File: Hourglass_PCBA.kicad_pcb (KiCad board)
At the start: 2 copper layers, 0.9 x 0.7 mm, 150 parts, among them J1 B2B-PH-SM4-TBLFSN, J2 UJ31-CH-G2-SMT-TR, J3 009159010061911, SW1 KMR221NGLFS, U1 STM32L432KCUx, U2 LP5860, U3 LSM6DSOXTR, U4 MCP1727T-3302E/SN, U5 BQ25185DLHR

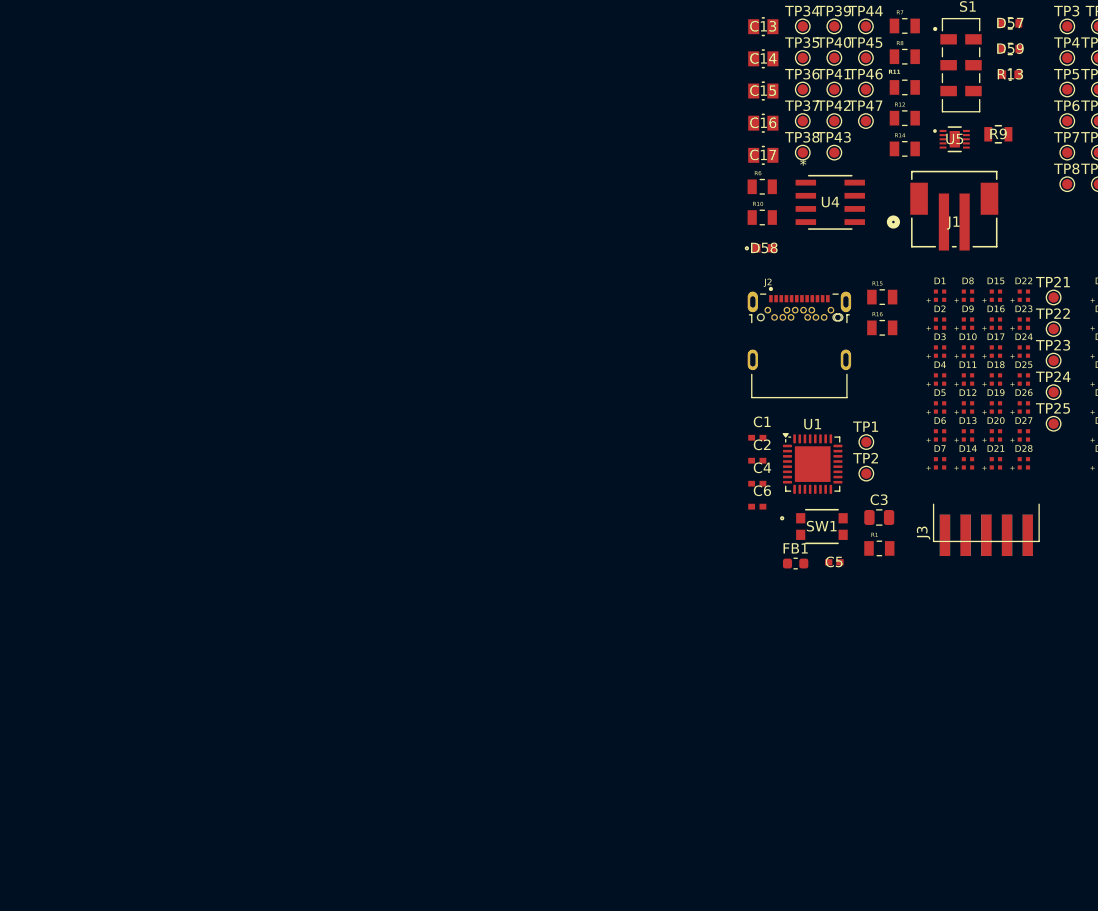
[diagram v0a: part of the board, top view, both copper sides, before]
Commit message: Addressed pull-up on NRST. Added GPIO for  VIO_EN. Added comments on schematic and some TPs
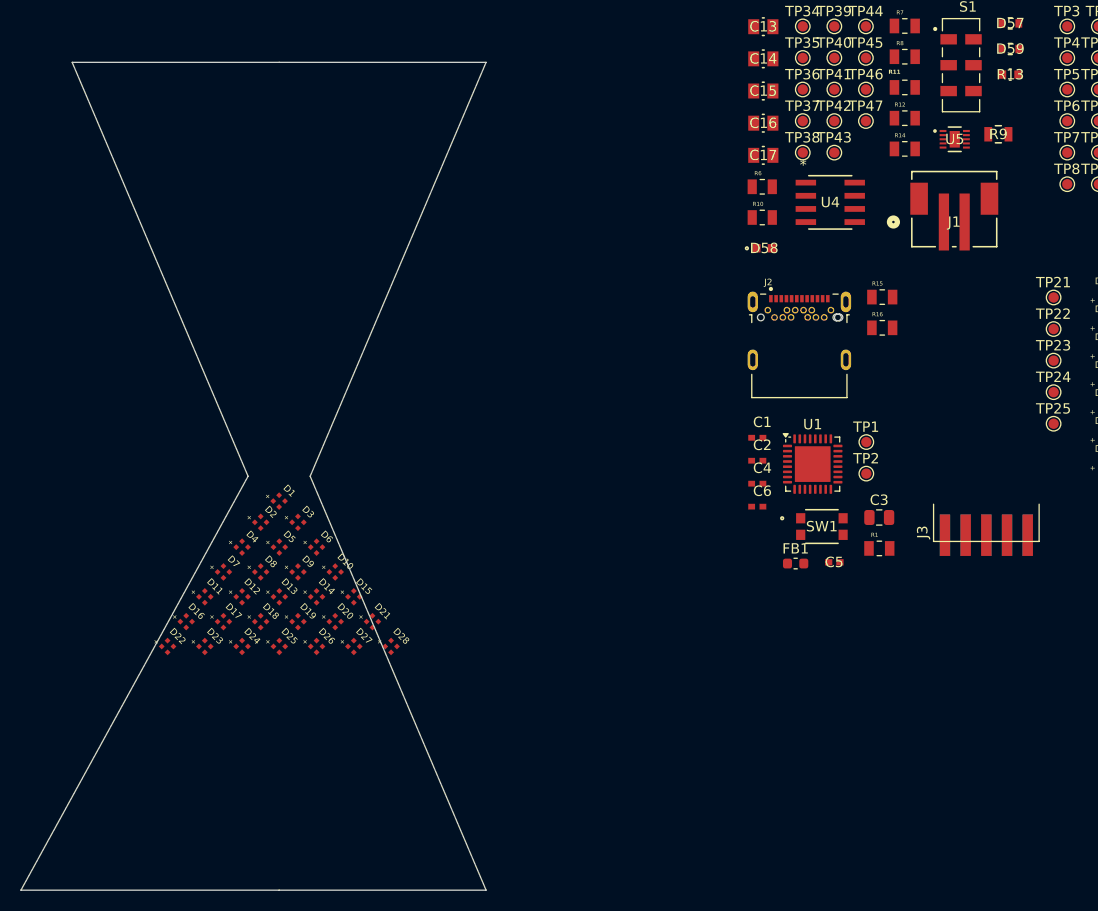
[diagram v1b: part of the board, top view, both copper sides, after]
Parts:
- moved D22 89.4 mm to (189.2, 216.4), turned to -45 degrees
- moved D23 85.1 mm to (192.8, 216.4), turned to -45 degrees
- moved D16 83.4 mm to (191.0, 214.1), turned to -45 degrees
- moved D24 80.7 mm to (196.4, 216.4), turned to -45 degrees
- moved D17 79.1 mm to (194.6, 214.1), turned to -45 degrees
- moved D11 76.7 mm to (192.8, 211.7), turned to -45 degrees
- moved D25 76.4 mm to (200.0, 216.4), turned to -45 degrees
- moved D18 74.8 mm to (198.2, 214.1), turned to -45 degrees
- moved D8 73.4 mm to (198.2, 209.2), turned to -45 degrees
- moved D12 72.5 mm to (196.4, 211.7), turned to -45 degrees
- moved D26 72.1 mm to (203.6, 216.4), turned to -45 degrees
- moved D19 70.6 mm to (201.8, 214.1), turned to -45 degrees
- moved D7 70.0 mm to (194.6, 209.2), turned to -45 degrees
- moved D4 69.4 mm to (196.4, 206.8), turned to -45 degrees
- moved D9 69.1 mm to (201.8, 209.2), turned to -45 degrees
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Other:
- board size 0.9 x 0.7 mm -> 44.9 x 80 mm

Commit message: Re-annotated entire schematic.
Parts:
- added R17: RC0805FR-075K1L, Hourglass_footprint_library:RC0805FR-075K1L, F.Cu at (320.3, 162.8)
- added TP48: TestPoint, TestPoint:TestPoint_Pad_D1.0mm, F.Cu at (316.8, 162.9)
- added TP49: TestPoint, TestPoint:TestPoint_Pad_D1.0mm, F.Cu at (316.8, 165.9)
- added TP50: TestPoint, TestPoint:TestPoint_Pad_D1.0mm, F.Cu at (307.1, 167.1)
- FB1: value FerriteBead_Small -> FCM 1608KF-601T03
- R1: value RMCF0805FT10K0 -> CRCW080518K0FKEAHP; footprint Hourglass_footprint_library:RMCF0805FT10K0 -> Hourglass_footprint_library:CRCW080518K0FKEAHP
- R10: value MCU08050C6000FP500 -> CRCW080518K0FKEAHP; footprint Hourglass_footprint_library:RESC2012X55N -> Hourglass_footprint_library:CRCW080518K0FKEAHP
- R11: value RC0805FR-07442RL -> MCU08050C6000FP500; footprint Hourglass_footprint_library:RC0805FR-07442RL -> Hourglass_footprint_library:RESC2012X55N
- R12: value RMCF0805FT10K0 -> RC0805FR-07442RL; footprint Hourglass_footprint_library:RMCF0805FT10K0 -> Hourglass_footprint_library:RC0805FR-07442RL
- R13: value RC0603JR-07300RL -> RMCF0805FT10K0; footprint Hourglass_footprint_library:RC0603N_YAG -> Hourglass_footprint_library:RMCF0805FT10K0
- R14: value RMCF0805FT10K0 -> RC0603JR-07300RL; footprint Hourglass_footprint_library:RMCF0805FT10K0 -> Hourglass_footprint_library:RC0603N_YAG
- R15: value RC0805FR-075K1L -> RMCF0805FT10K0; footprint Hourglass_footprint_library:RC0805FR-075K1L -> Hourglass_footprint_library:RMCF0805FT10K0
- R2, R3: value RMCF0805FT10K0 -> CRGCQ0805F4K7; footprint Hourglass_footprint_library:RMCF0805FT10K0 -> Hourglass_footprint_library:CRGCQ0805F4K7
- R6: value MCU08050C6000FP500 -> RMCF0805FT10K0; footprint Hourglass_footprint_library:RESC2012X55N -> Hourglass_footprint_library:RMCF0805FT10K0
- R7: value RCS0805300RFKEA -> MCU08050C6000FP500; footprint Hourglass_footprint_library:RCS0805300RFKEA -> Hourglass_footprint_library:RESC2012X55N
- R8: value RCS080513K0FKEA -> RCS0805300RFKEA; footprint Hourglass_footprint_library:RCS080513K0FKEA -> Hourglass_footprint_library:RCS0805300RFKEA
- R9: value CRCW080518K0FKEAHP -> RCS080513K0FKEA; footprint Hourglass_footprint_library:CRCW080518K0FKEAHP -> Hourglass_footprint_library:RCS080513K0FKEA
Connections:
- C9 pad 1: +3V3 -> /LED Driver +  LEDs/VIO_EN
- R1 pad 1: GND -> /MCU/NRST
- R1 pad 2: /MCU/BOOT -> +3V3
- R10 pad 1: Net-(D57-Pad2) -> GND
- R10 pad 2: VCC -> Net-(R10-Pad2)
- R11 pad 1: Net-(D58-Pad2) -> Net-(D57-Pad2)
- R12 pad 1: Net-(U4-PWRGD) -> Net-(D58-Pad2)
- R12 pad 2: +3V3 -> VCC
- R13 pad 1: Net-(D59-Pad1) -> Net-(U4-PWRGD)
- R14 pad 1: GND -> Net-(D59-Pad1)
- R14 pad 2: Net-(U5-TS/MR) -> +3V3
- R15 pad 2: Net-(J2-CC2) -> Net-(U5-TS/MR)
- R16 pad 2: Net-(J2-CC1) -> Net-(J2-CC2)
- R2 pad 1: /LED Driver +  LEDs/I2C.SDA -> /LED Driver +  LEDs/I2C.SCL
- R3 pad 1: /LED Driver +  LEDs/I2C.SCL -> /LED Driver +  LEDs/I2C.SDA
- R4 pad 1: Net-(U3-CS) -> GND
- R4 pad 2: +3V3 -> /MCU/BOOT
- R5 pad 1: GND -> Net-(U3-CS)
- R5 pad 2: Net-(U3-SDO/SA0) -> +3V3
- R6 pad 2: Net-(R6-Pad2) -> Net-(U3-SDO/SA0)
- S1 pad 1: Net-(R6-Pad2) -> Net-(R7-Pad2)
- S1 pad 3: Net-(R7-Pad2) -> Net-(R8-Pad2)
- S1 pad 5: Net-(R9-Pad2) -> Net-(R10-Pad2)
- S1 pad 7: Net-(R8-Pad2) -> Net-(R9-Pad2)
- TP10 pad 1: /LED Driver +  LEDs/CS7 -> /LED Driver +  LEDs/CS13
- TP11 pad 1: /LED Driver +  LEDs/CS8 -> /LED Driver +  LEDs/CS12
- TP12 pad 1: /LED Driver +  LEDs/CS9 -> /LED Driver +  LEDs/CS11
- TP14 pad 1: /LED Driver +  LEDs/CS11 -> /LED Driver +  LEDs/CS9
- TP15 pad 1: /LED Driver +  LEDs/CS12 -> /LED Driver +  LEDs/CS8
- TP16 pad 1: /LED Driver +  LEDs/CS13 -> /LED Driver +  LEDs/CS7
- TP17 pad 1: /LED Driver +  LEDs/CS14 -> /LED Driver +  LEDs/CS6
- TP18 pad 1: /LED Driver +  LEDs/CS15 -> /LED Driver +  LEDs/CS5
- TP19 pad 1: /LED Driver +  LEDs/CS16 -> /LED Driver +  LEDs/CS4
- TP20 pad 1: /LED Driver +  LEDs/CS17 -> /LED Driver +  LEDs/CS3
- TP21 pad 1: /LED Driver +  LEDs/SW0 -> /LED Driver +  LEDs/CS2
- TP22 pad 1: /LED Driver +  LEDs/SW1 -> /LED Driver +  LEDs/CS1
- TP23 pad 1: /LED Driver +  LEDs/SW2 -> /LED Driver +  LEDs/CS0
- TP24 pad 1: /LED Driver +  LEDs/SW3 -> /LED Driver +  LEDs/SW0
- TP25 pad 1: /LED Driver +  LEDs/SW4 -> /LED Driver +  LEDs/SW1
- TP26 pad 1: /LED Driver +  LEDs/SW5 -> /LED Driver +  LEDs/SW2
- TP27 pad 1: /LED Driver +  LEDs/SW6 -> /LED Driver +  LEDs/SW3
- TP28 pad 1: /LED Driver +  LEDs/SW7 -> /LED Driver +  LEDs/SW4
- TP29 pad 1: /LED Driver +  LEDs/SW8 -> /LED Driver +  LEDs/SW5
- TP3 pad 1: /LED Driver +  LEDs/CS0 -> /LED Driver +  LEDs/I2C.SCL
- TP30 pad 1: /LED Driver +  LEDs/SW9 -> /LED Driver +  LEDs/SW6
- TP31 pad 1: /LSM6DSOX 6-Axis IMU/LSM6DSOX_INT2 -> /LED Driver +  LEDs/SW7
- TP32 pad 1: /LSM6DSOX 6-Axis IMU/LSM6DSOX_INT1 -> /LED Driver +  LEDs/SW8
- TP33 pad 1: Net-(U3-CS) -> /LED Driver +  LEDs/SW9
- TP34 pad 1: VCC -> /LSM6DSOX 6-Axis IMU/LSM6DSOX_INT2
- TP35 pad 1: Net-(U5-STAT1) -> /LSM6DSOX 6-Axis IMU/LSM6DSOX_INT1
- TP36 pad 1: GND -> Net-(U3-CS)
- TP37 pad 1: Net-(U5-STAT2) -> VCC
- TP38 pad 1: +3V3 -> Net-(U5-STAT1)
- TP39 pad 1: /Power/ILIM/VSET -> GND
- TP4 pad 1: /LED Driver +  LEDs/CS1 -> /LED Driver +  LEDs/I2C.SDA
- TP40 pad 1: Net-(U4-*SHDN) -> Net-(U5-STAT2)
- TP41 pad 1: /Power/ISET -> +3V3
- TP42 pad 1: Net-(U4-PWRGD) -> /Power/ILIM/VSET
- TP43 pad 1: Net-(U5-BAT) -> Net-(U4-*SHDN)
- TP44 pad 1: GND -> /Power/ISET
- TP45 pad 1: GND -> Net-(U4-PWRGD)
- TP46 pad 1: GND -> Net-(U5-BAT)
- TP5 pad 1: /LED Driver +  LEDs/CS2 -> /LED Driver +  LEDs/VIO_EN
- TP6 pad 1: /LED Driver +  LEDs/CS3 -> /LED Driver +  LEDs/CS17
- TP7 pad 1: /LED Driver +  LEDs/CS4 -> /LED Driver +  LEDs/CS16
- TP8 pad 1: /LED Driver +  LEDs/CS5 -> /LED Driver +  LEDs/CS15
- TP9 pad 1: /LED Driver +  LEDs/CS6 -> /LED Driver +  LEDs/CS14
- U1 pad 28: unconnected-(U1-PB5-Pad28) -> /LED Driver +  LEDs/VIO_EN
- U2 pad 39: +3V3 -> /LED Driver +  LEDs/VIO_EN

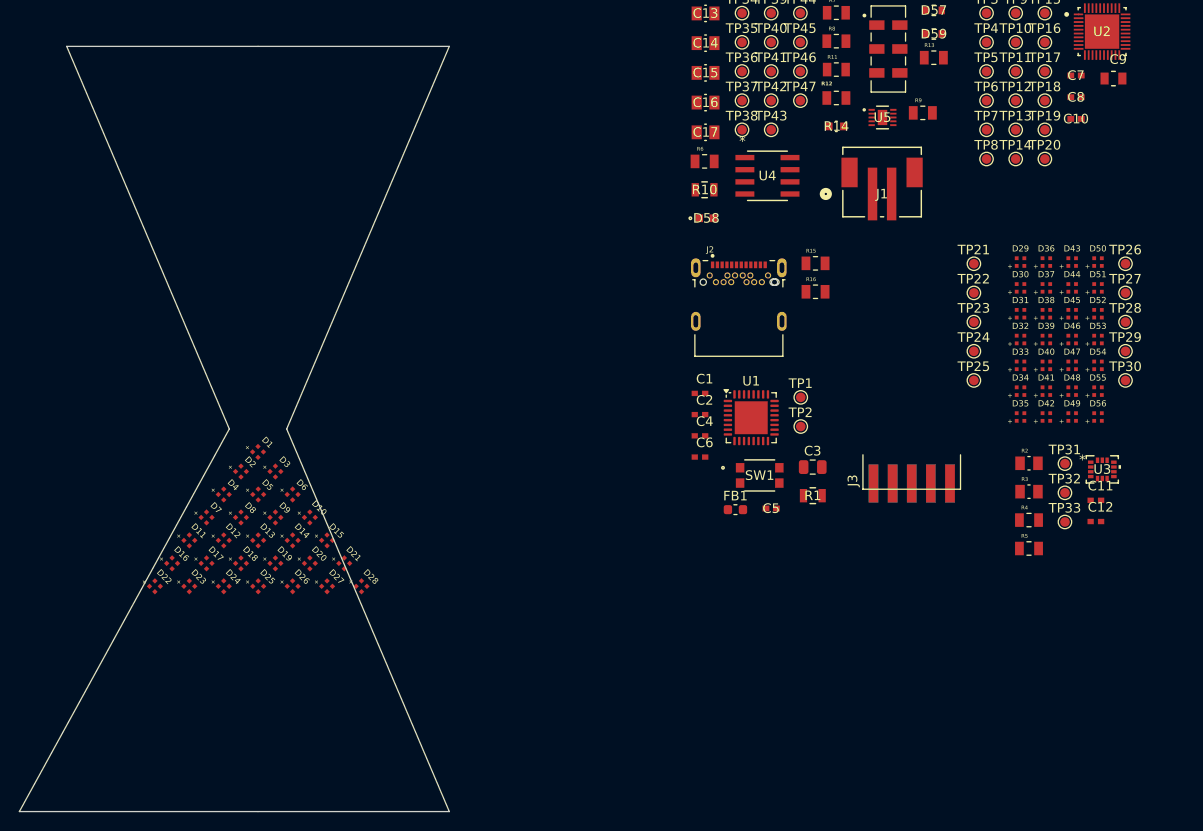
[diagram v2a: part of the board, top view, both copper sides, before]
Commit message: Aligned all LEDs
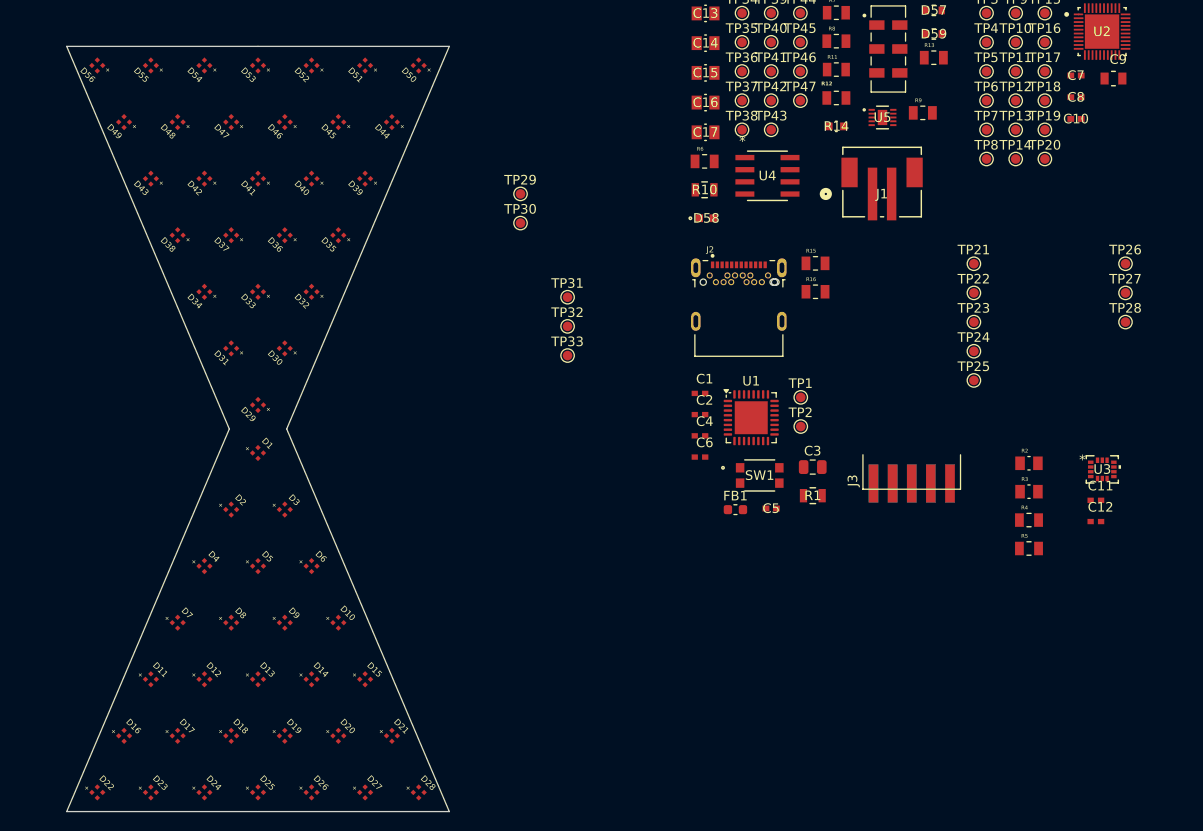
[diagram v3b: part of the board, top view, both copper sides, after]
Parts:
- moved D56 110.9 mm to (183.2, 162.0), turned to 135 degrees
- moved D55 104.7 mm to (188.8, 162.0), turned to 135 degrees
- moved D49 103.8 mm to (186.0, 167.9), turned to 135 degrees
- moved D54 98.5 mm to (194.4, 162.0), turned to 135 degrees
- moved D48 97.7 mm to (191.6, 167.9), turned to 135 degrees
- moved D43 96.7 mm to (188.8, 173.8), turned to 135 degrees
- moved D53 92.4 mm to (200.0, 162.0), turned to 135 degrees
- moved D47 91.5 mm to (197.2, 167.9), turned to 135 degrees
- moved D42 91.5 mm to (194.4, 173.8), turned to 135 degrees
- moved D38 91.2 mm to (191.6, 179.7), turned to 135 degrees
- moved D52 86.2 mm to (205.6, 162.0), turned to 135 degrees
- moved D34 86.0 mm to (194.4, 185.7), turned to 135 degrees
- moved D46 85.4 mm to (202.8, 167.9), turned to 135 degrees
- moved D37 85.4 mm to (197.2, 179.7), turned to 135 degrees
- moved D41 85.4 mm to (200.0, 173.8), turned to 135 degrees
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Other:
- board size 44.9 x 80 mm -> 40 x 80 mm

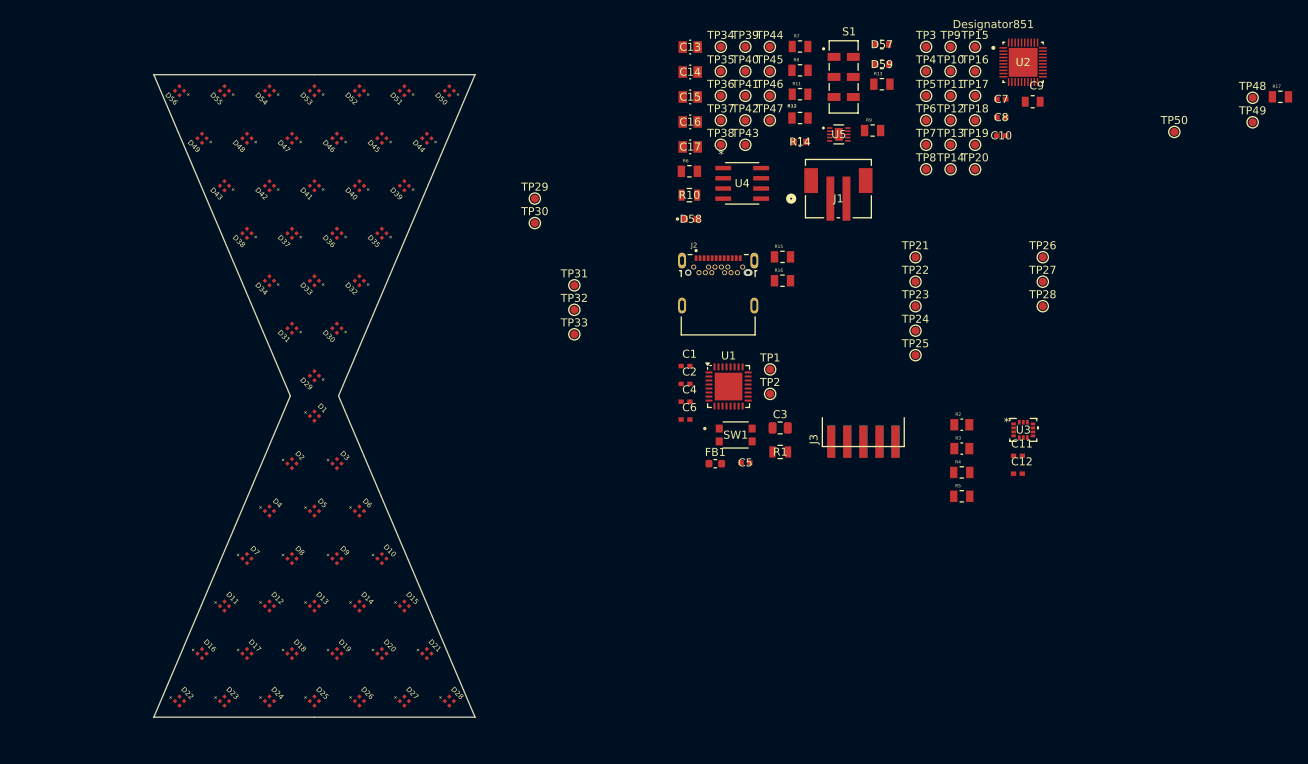
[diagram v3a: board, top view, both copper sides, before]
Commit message: Arranged parts for power- not complete at this commit.
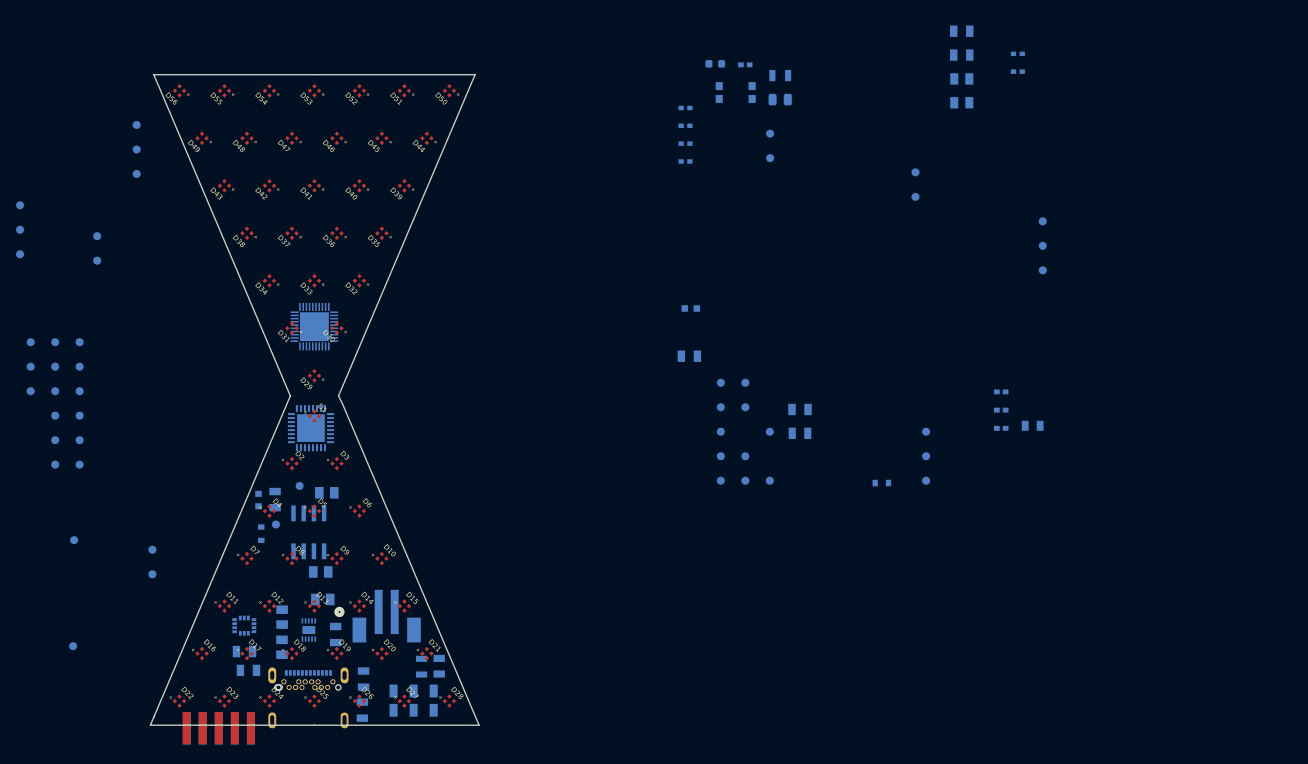
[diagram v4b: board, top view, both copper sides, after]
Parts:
- C1, C10, C11, C12, C13, C14, C15, C16, C17, C2, C3, C4, C5, C6, C7, C8, C9, D57, D58, D59, FB1, J1, J2, J3, R1, R10, R11, R12, R13, R14, R15, R16, R17, R2, R3, R4, R5, R6, R7, R8, R9, S1, SW1, TP1, TP10, TP11, TP12, TP13, TP14, TP15, TP16, TP17, TP18, TP19, TP2, TP20, TP21, TP22, TP23, TP24, TP25, TP26, TP27, TP28, TP29, TP3, TP30, TP31, TP32, TP33, TP34, TP35, TP36, TP37, TP38, TP39, TP4, TP40, TP41, TP42, TP43, TP44, TP45, TP46, TP47, TP48, TP49, TP5, TP50, TP6, TP7, TP8, TP9, U1, U2, U3, U4, U5: moved to B.Cu
- moved TP48 149.3 mm to (179.8, 222.2)
- moved TP49 147.0 mm to (179.8, 219.2)
- moved R17 146.3 mm to (191.3, 231.8)
- moved TP50 146.1 mm to (170.1, 218.0)
- moved TP15 123.0 mm to (170.8, 208.6)
- moved TP9 123.0 mm to (167.7, 208.6)
- moved TP16 120.6 mm to (170.8, 205.5)
- moved TP10 120.6 mm to (167.7, 205.5)
- moved TP17 118.4 mm to (170.8, 202.5)
- moved TP11 118.4 mm to (167.7, 202.5)
- moved TP6 116.5 mm to (164.7, 199.4)
- moved TP18 116.5 mm to (170.8, 199.4)
- moved TP12 116.5 mm to (167.7, 199.4)
- moved TP7 114.9 mm to (164.7, 196.4)
- moved TP13 114.9 mm to (167.7, 196.4)
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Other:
- board size 40 x 80 mm -> 40.9 x 81 mm

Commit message: Moved all TPs to board area except CS TPs. Deleted some TPs that are less of a priority.
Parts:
- removed TP49, TP50: TestPoint, TestPoint:TestPoint_Pad_D1.0mm
- TP39: moved to F.Cu
- moved TP39 344.4 mm to (-11.5, -9.17)
- moved TP26 113.7 mm to (186.2, 229.1)
- moved TP25 98.2 mm to (191.1, 223.4)
- moved TP28 96.0 mm to (218.2, 241.3)
- moved C11 92.5 mm to (195.1, 162.8), turned to -90 degrees
- moved TP27 91.0 mm to (213.2, 229.1)
- moved C12 90.9 mm to (196.8, 162.9), turned to -90 degrees
- moved C9 90.8 mm to (198.7, 203.5), turned to -90 degrees
- moved TP3 88.7 mm to (199.2, 166.6)
- moved TP4 85.6 mm to (199.4, 169.5)
- moved C10 84.3 mm to (201.3, 203.5), turned to -90 degrees
- moved C8 83.3 mm to (202.5, 209.0)
- moved C7 83.1 mm to (202.5, 207.5)
- moved J3 82.8 mm to (194.8, 159.2), turned to 180 degrees
- moved TP47 81.4 mm to (208.5, 159.4)
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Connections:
- TP39 pad 1: GND -> Net-(U5-STAT2)
- TP40 pad 1: Net-(U5-STAT2) -> +3V3
- TP41 pad 1: +3V3 -> /Power/ILIM/VSET
- TP42 pad 1: /Power/ILIM/VSET -> Net-(U4-*SHDN)
- TP43 pad 1: Net-(U4-*SHDN) -> /Power/ISET
- TP44 pad 1: /Power/ISET -> Net-(U5-BAT)
- TP45 pad 1: Net-(U4-PWRGD) -> GND
- TP46 pad 1: Net-(U5-BAT) -> GND
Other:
- board size 40.9 x 81 mm -> 40.9 x 87.5 mm
